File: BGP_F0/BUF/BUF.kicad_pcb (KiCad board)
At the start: 2 copper layers, 30 x 30 mm, 34 parts, among them P1 CONN_01X02, P2 CONN_01X02, P3 CONN_01X03, P4 CONN_01X02, P5 CONN_01X02, P6 CONN_01X09, P7 CONN_01X03, P8 CONN_01X05, Q1 2SK208, Q2 2SK208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

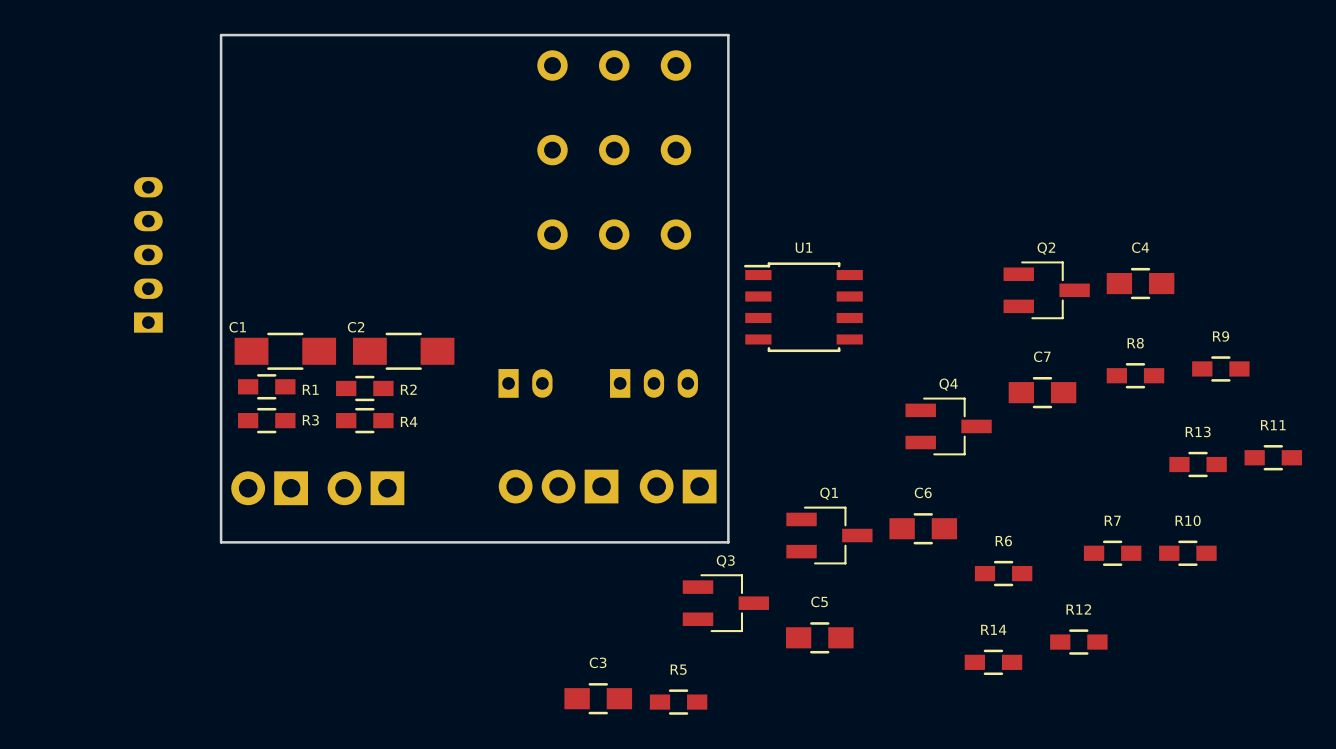
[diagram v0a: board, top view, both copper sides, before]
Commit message: F0 Buffer Board
Buffer done.  30mm x 40mm, with optional outboard volume or concentric vol/blend.  Output bypass EQ and straight to output possible.
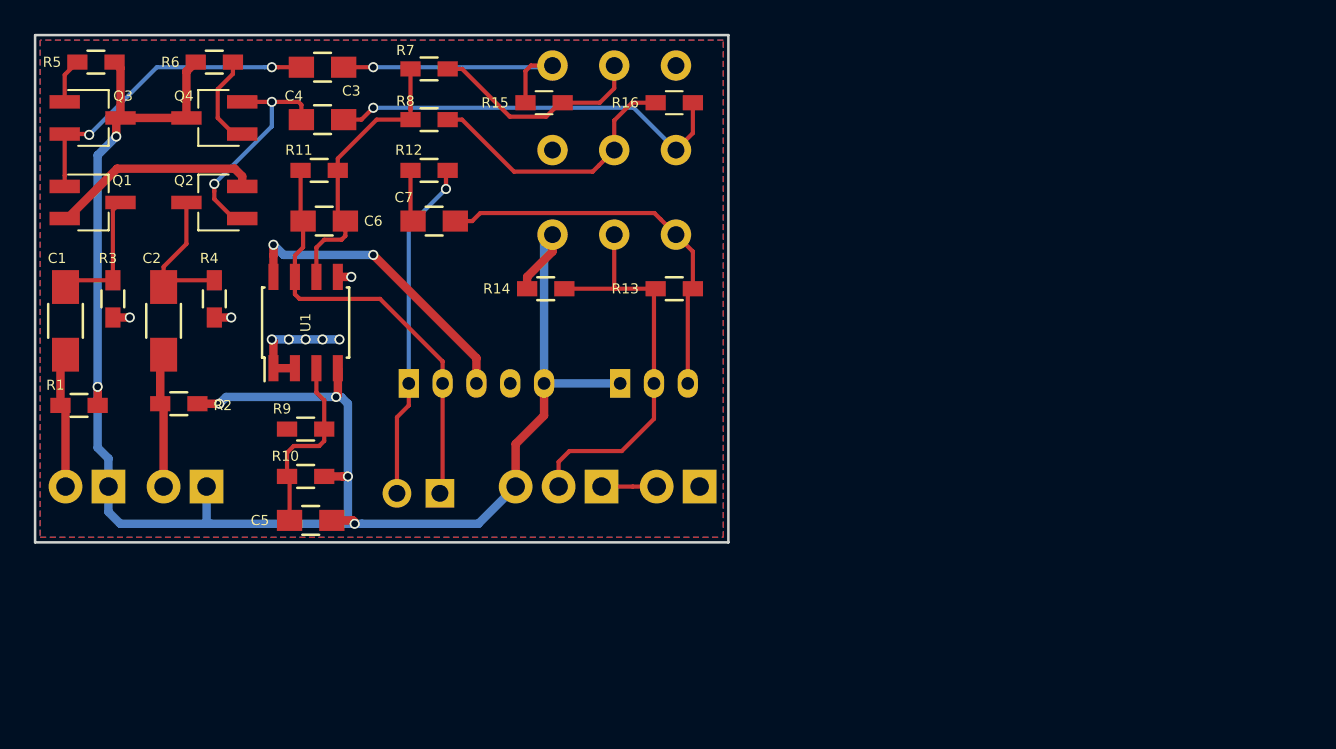
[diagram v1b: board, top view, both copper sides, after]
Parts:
- added R15: 499k, Resistors_SMD:R_0603_HandSoldering, F.Cu at (152.1, 82.0)
- added R16: 499k, Resistors_SMD:R_0603_HandSoldering, F.Cu at (159.8, 82.0)
- P5: footprint Connectors_JST:JST_PH_B2B-PH-K_02x2.00mm_Straight -> Pin_Headers:Pin_Header_Straight_1x02_Pitch2.54mm
- R11, R7, R8: value 499k -> 4.99k
- moved R11 58.9 mm to (138.8, 86.0)
- moved R6 55.6 mm to (132.6, 79.6), turned to 180 degrees
- moved R9 54.2 mm to (138.0, 101.3)
- moved R10 52.4 mm to (138.0, 104.1)
- moved R5 51.2 mm to (125.6, 79.6)
- moved R7 49.5 mm to (145.3, 80.0)
- moved Q2 49.5 mm to (132.6, 87.9), turned to 180 degrees
- moved C4 49.3 mm to (139.0, 83.0)
- moved Q1 47.8 mm to (125.4, 87.9)
- moved R12 47.5 mm to (145.3, 86.0)
- moved Q3 47.2 mm to (125.4, 82.9)
- moved Q4 47.1 mm to (132.6, 82.9), turned to 180 degrees
- moved R8 44.4 mm to (145.3, 83.0)
- moved C3 40.7 mm to (139.0, 79.9)
- moved C6 39.8 mm to (139.1, 89.0)
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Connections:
- C1 pad 2: Net-(C1-Pad2) -> /IN_B
- C2 pad 2: Net-(C2-Pad2) -> /IN_N
- P4 pad 1: /BAT+ -> /V+
- R1 pad 1: Net-(C1-Pad2) -> /IN_B
- R2 pad 1: Net-(C2-Pad2) -> /IN_N
- U1 pad 1: Net-(U1-Pad1) -> /VRef
- U1 pad 2: Net-(U1-Pad1) -> /VRef
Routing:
- net Earth: track 0.00 -> 108.7 mm, vias 0 -> 6
- net /V+: track 0.00 -> 31.3 mm, vias 0 -> 2
- net /OUT_BUF: track 0.00 -> 25.8 mm
- net /PV_2: track 0.00 -> 24.5 mm
- net /PB2_3: track 0.00 -> 24.2 mm, vias 0 -> 1
- net /PV_3: track 0.00 -> 23.1 mm
- net /IN_EQ: track 0.00 -> 20.3 mm, vias 0 -> 1
- net Net-(C3-Pad1): track 0.00 -> 18.8 mm, vias 0 -> 2
- net Net-(C6-Pad2): track 0.00 -> 17.3 mm
- net /PB2_2: track 0.00 -> 16.3 mm
- net /PB1_1: track 0.00 -> 16.0 mm, vias 0 -> 1
- net Net-(C4-Pad1): track 0.00 -> 13.7 mm, vias 0 -> 2
- net /PB1_2: track 0.00 -> 13.1 mm
- net Net-(C5-Pad1): track 0.00 -> 11.0 mm
- net /VRef: track 0.00 -> 9.80 mm, vias 0 -> 8
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- added copper zone on F.Cu, net /V+
- added copper zone on B.Cu, net /VRef
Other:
- board size 30 x 30 mm -> 41 x 30 mm
- net class Default: clearance 0.2 -> 0.25
- net class PWR added: clearance 0.25, trace_width 0.5, via_dia 0.6, via_drill 0.4
- rule trace_clearance: 0.2 -> 0.25
- rule trace_min: 0.2 -> 0.25

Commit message: clranup
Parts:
- moved C5 0.89 mm to (137.8, 106.0)
- moved R10 0.85 mm to (137.7, 103.3)
- moved R9 0.58 mm to (137.7, 100.8)
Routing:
- net /V+: track 31.3 -> 40.6 mm
- net Net-(C5-Pad1): track 11.0 -> 9.41 mm

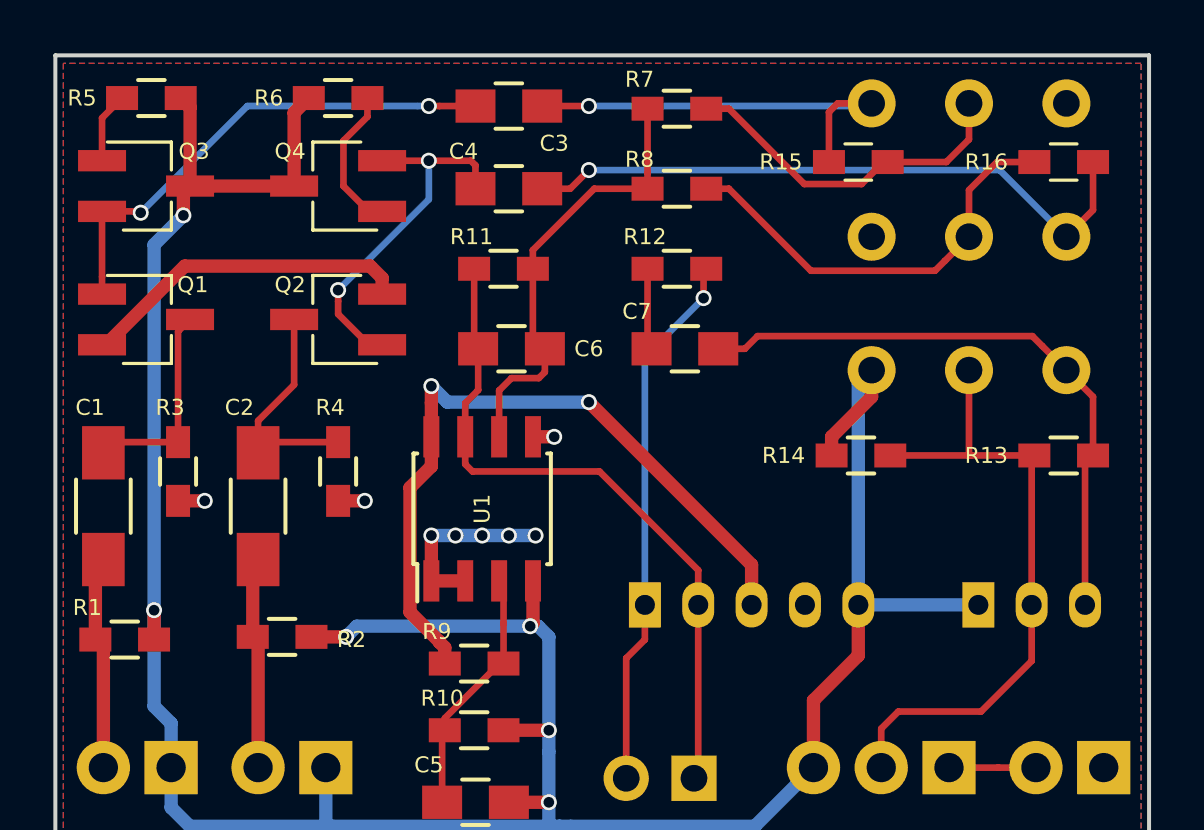
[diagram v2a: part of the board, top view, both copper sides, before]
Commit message: Added BT and MID. Mid not layed out yet
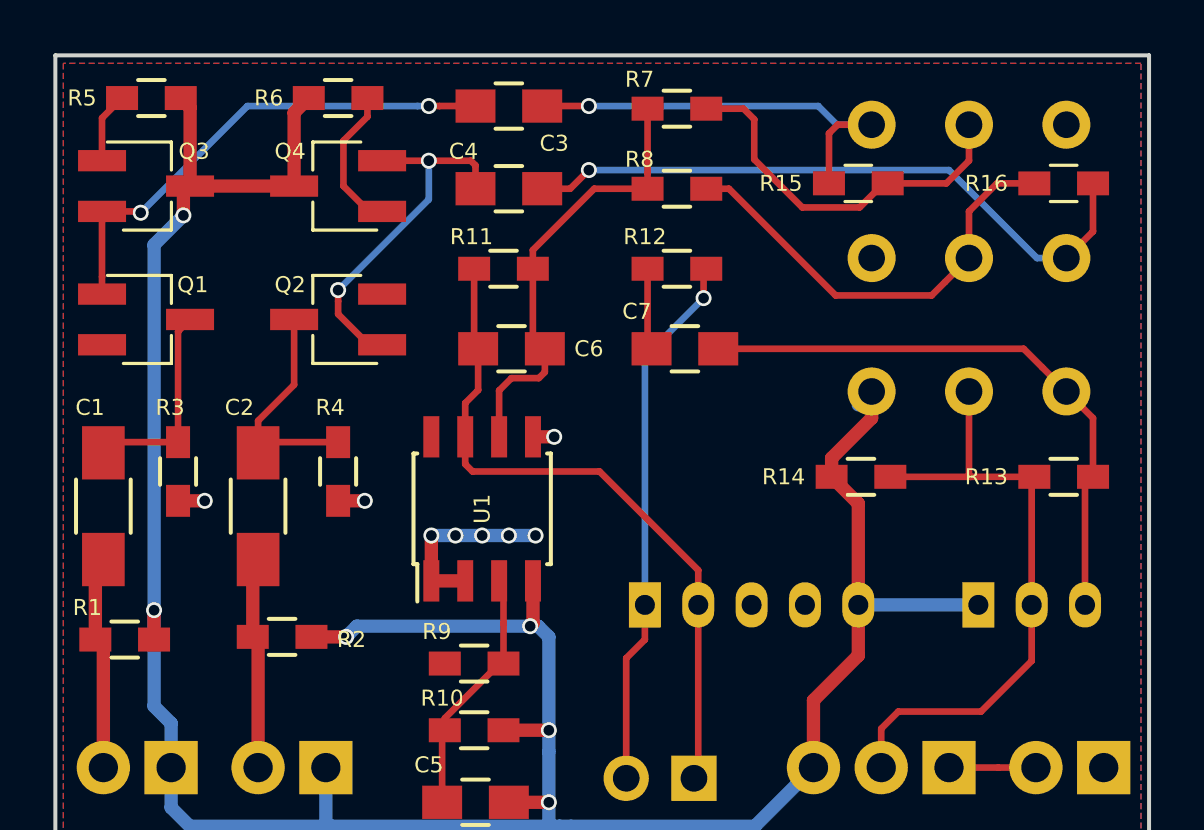
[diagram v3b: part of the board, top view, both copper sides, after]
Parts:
- moved P6 0.80 mm to (152.6, 80.6)
- moved R13 0.80 mm to (159.8, 93.8)
- moved R14 0.80 mm to (152.2, 93.8)
- moved R15 0.80 mm to (152.1, 82.8)
- moved R16 0.80 mm to (159.8, 82.8)
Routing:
- net /V+: track 40.6 -> 0.90 mm, vias 2 -> 0
- net Earth: track 109.0 -> 105.9 mm
- net /PB1_2: track 13.1 -> 14.3 mm
- net /PV_3: track 23.1 -> 22.3 mm
- net /PV_2: track 24.5 -> 23.7 mm

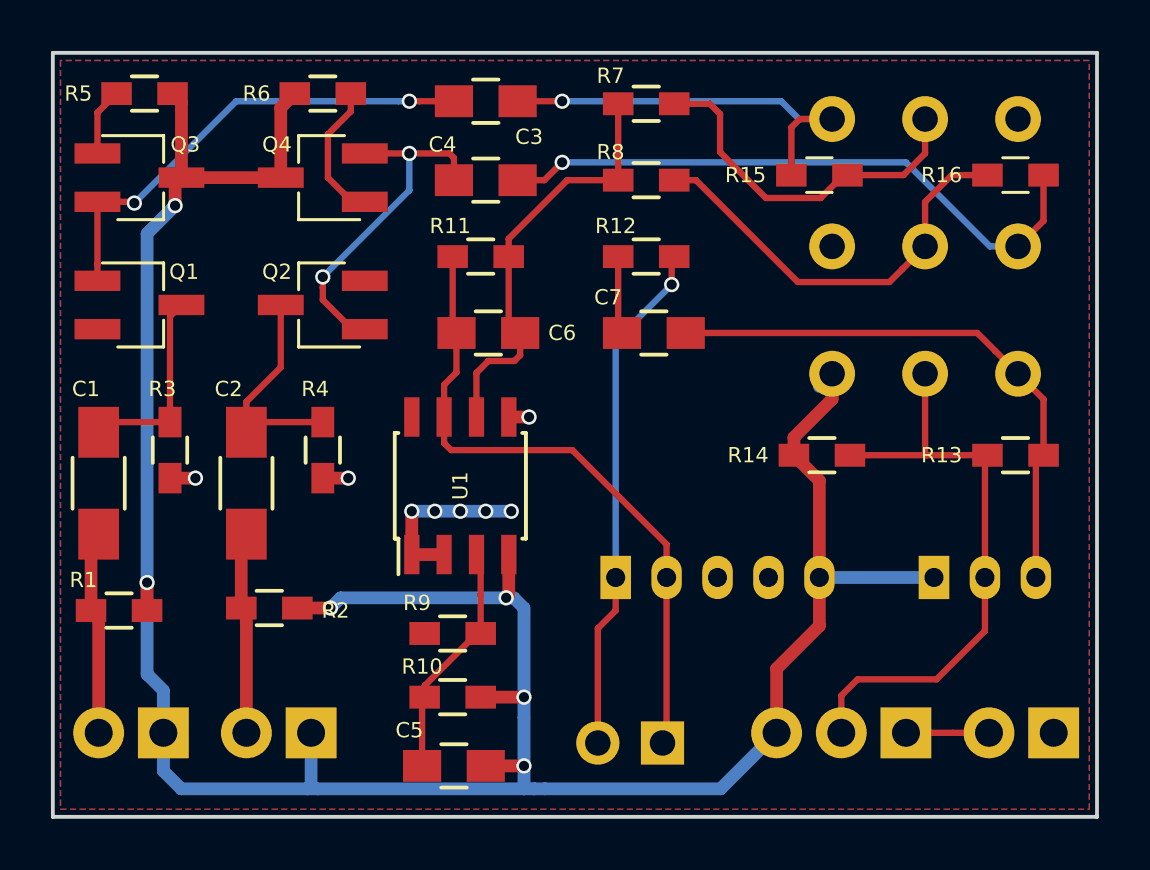
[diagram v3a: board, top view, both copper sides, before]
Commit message: F0 BUF is now 26x40
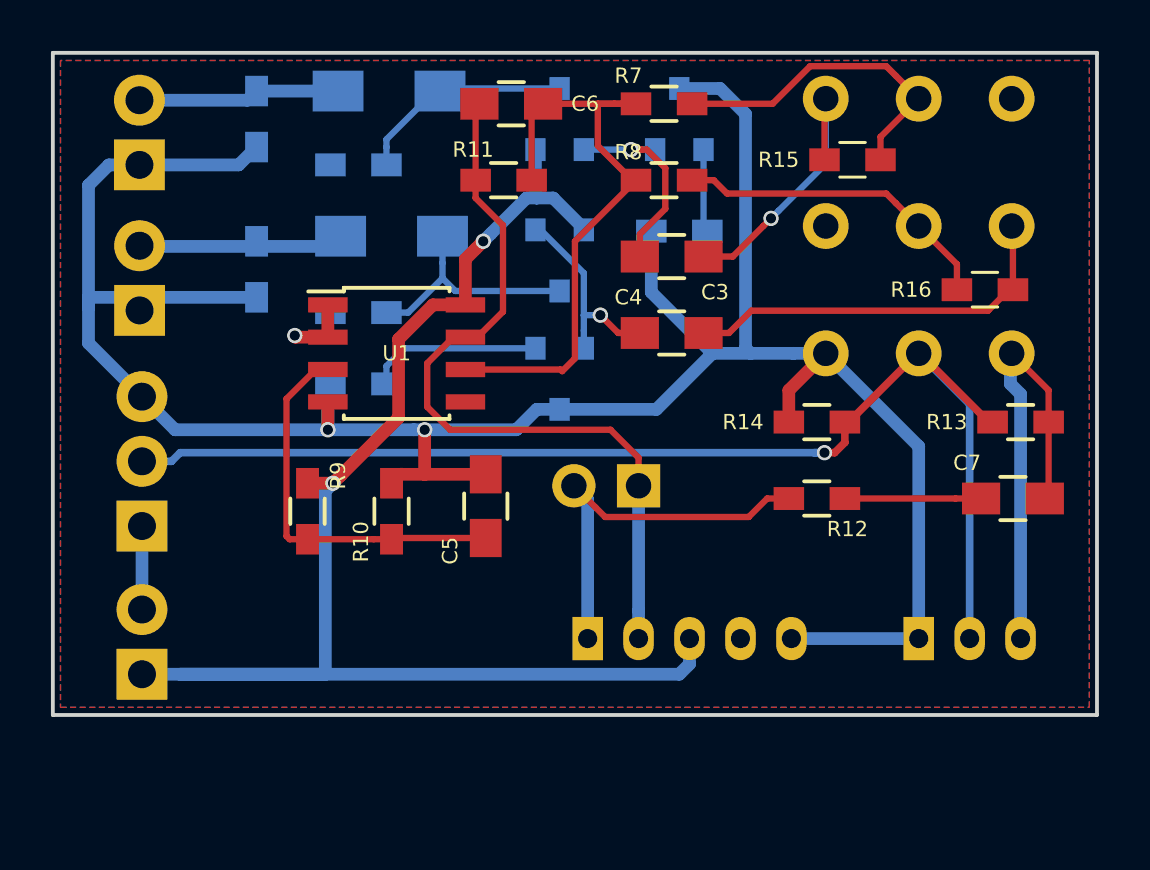
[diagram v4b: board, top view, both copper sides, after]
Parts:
- C1, C2, R1, R2, R3, R4, R5, R6: moved to B.Cu
- Q1, Q2, Q3, Q4: footprint TO_SOT_Packages_SMD:SC-59_Handsoldering -> TO_SOT_Packages_SMD:SC-59; moved to B.Cu
- moved P4 35.9 mm to (125.5, 102.4), turned to 90 degrees
- moved P3 31.1 mm to (125.5, 96.6), turned to 90 degrees
- moved P1 22.3 mm to (125.4, 82.4), turned to 90 degrees
- moved R5 21.7 mm to (146.6, 85.0), turned to 180 degrees
- moved Q3 21.3 mm to (146.6, 80.6), turned to 90 degrees
- moved R1 20.0 mm to (130.0, 80.6), turned to 270 degrees
- moved C1 19.2 mm to (135.2, 79.5), turned to 180 degrees
- moved Q1 18.0 mm to (141.9, 80.6), turned to 90 degrees
- moved P2 17.9 mm to (125.4, 88.1), turned to 90 degrees
- moved C7 15.5 mm to (159.7, 95.5)
- moved R3 13.4 mm to (134.0, 82.4), turned to 180 degrees
- moved R2 13.3 mm to (130.0, 86.5), turned to 270 degrees
- moved Q4 12.2 mm to (141.9, 90.8), turned to 270 degrees
- moved R12 11.6 mm to (152.0, 95.5), turned to 180 degrees
- moved R6 11.5 mm to (134.0, 91.0)
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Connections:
- C1 pad 2: /IN_B -> /IN_N
- C2 pad 2: /IN_N -> /IN_B
- C6 pad 1: /OUT_BUF -> /IN_EQ
- P1 pad 2: /IN_B -> /IN_N
- P2 pad 2: /IN_N -> /IN_B
- P5 pad 1: /OUT_BUF -> /IN_EQ
- P5 pad 2: /IN_EQ -> /OUT_EQ
- P8 pad 1: /IN_EQ -> /OUT_EQ
- P8 pad 2: /OUT_BUF -> /IN_EQ
- R1 pad 1: /IN_B -> /IN_N
- R11 pad 1: /OUT_BUF -> /IN_EQ
- R12 pad 2: /IN_EQ -> /OUT_EQ
- R2 pad 1: /IN_N -> /IN_B
- U1 pad 7: /OUT_BUF -> /IN_EQ
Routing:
- net /V+: track 0.90 -> 56.9 mm, vias 0 -> 2
- net /OUT_BUF: track 25.8 -> 0.00 mm
- net /PV_2: track 23.7 -> 49.2 mm, vias 0 -> 1
- net /OUT_EQ: track 0.00 -> 15.5 mm
- net /IN_EQ: track 20.3 -> 30.4 mm, vias 1 -> 0
- net Net-(C3-Pad1): track 18.8 -> 9.29 mm, vias 2 -> 1
- net /PB2_3: track 24.5 -> 15.4 mm, vias 1 -> 0
- net Net-(C6-Pad2): track 17.3 -> 24.6 mm
- net /VRef: track 9.67 -> 2.62 mm, vias 8 -> 1
- net Earth: track 105.9 -> 99.7 mm, vias 6 -> 2
- net Net-(C5-Pad1): track 9.41 -> 15.4 mm
- net Net-(C4-Pad1): track 13.7 -> 8.04 mm, vias 2 -> 1
- net /PB1_1: track 16.4 -> 11.3 mm
- net /PV_3: track 22.3 -> 18.2 mm
- net /PB2_2: track 16.7 -> 12.8 mm
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- added copper zone on F.Cu, net /VRef
- removed copper zone on F.Cu, net /V+
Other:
- board size 41 x 30 mm -> 41 x 26 mm
